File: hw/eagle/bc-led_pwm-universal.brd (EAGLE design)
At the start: 100 x 80 mm, 86 parts, among them T1 IRF7413, T10 IRF7413, T11 IRF7413, T12 IRF7413, T13 IRF7413, T14 IRF7413, T15 IRF7413, T16 IRF7413, T17 FDC6318P, T2 IRF7413, T3 IRF7413, T4 IRF7413, T5 IRF7413, T6 IRF7413, T7 IRF7413, T8 IRF7413, T9 IRF7413

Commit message: rotate core module to have convenient access to USB port, added pull-down resistors on output FETs, proper VDD_OFF handling and added power outage monitoring via P17
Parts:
- removed R2: 560R, resistor:R2012
- removed R3: 10k, resistor:R2012
- removed T17: FDC6318P, mixi:SSOT6
- added D2, D3, D4: B340A, diode:MELF-MLL41
- added R21, R22, R23, R24, R25, R26, R27, R28, R29, R30, R43, R44, R45, R46, R47, R48: 10k, resistor:R3216
- added R49: 560R, resistor:R3216
- R1: value 100k -> 560R; device resistor:R2012 -> resistor:R3216
- R4: device resistor:R2012 -> resistor:R3216
- moved R1 38.2 mm to (44.5, 54.6), turned to 90 degrees
- moved R4 32.0 mm to (88.9, 67.3)
- moved R8 26.2 mm to (43.2, 69.8), turned to 270 degrees
- moved R9 20.8 mm to (40.6, 69.8), turned to 270 degrees
- moved R19 14.2 mm to (34.3, 69.8), turned to 270 degrees
- moved R20 12.7 mm to (31.8, 69.8), turned to 270 degrees
- moved U$1 5.08 mm to (86.4, 53.3)
- moved D1 3.81 mm to (86.4, 38.1)
- moved L1 2.54 mm to (86.4, 34.3)
- moved CORE 0.27 mm to (27.6, 63.2), turned to 270 degrees
- moved R65 0.25 mm to (70.9, 21.6)
- moved R83 0.25 mm to (81.0, 21.6)
- moved R11 0.25 mm to (20.1, 21.6)
- moved R17 0.25 mm to (30.2, 21.6)
- moved R35 0.25 mm to (40.4, 21.6)
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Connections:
- removed net N$1: R1.2, T17.2, T17.5
- removed net N$3: R1.1, R2.2, R3.1, T17.1, T17.3
- new net N$14: D2.C, R4.2
- new net N$15: D3.C, R49.2
- net +3V3: now also D2.A, D3.A, D4.A, R1.2; no longer R4.2, T17.6
- net GND: now also R21.1, R22.1, R23.1, R24.1, R25.1, R26.1, R27.1, R28.1, R29.1, R30.1, R43.1, R44.1, R45.1, R46.1, R47.1, R48.1; no longer R3.2
- net N$10: now also R22.2
- net N$12: now also R24.2
- net N$2: now also R21.2
- net N$22: now also R25.2
- net N$24: now also R26.2
- net N$26: now also R27.2
- net N$28: now also R28.2
- net N$38: now also R29.2
- net N$40: now also R30.2
- net N$42: now also R43.2
- net N$44: now also R44.2
- net N$54: now also R45.2
- net N$56: now also R46.2
- net N$58: now also R47.2
- net N$60: now also R48.2
- net N$8: now also R23.2
- net P16: now also JP3.2
- net P17: now also R1.1; no longer JP3.2
- net VDD: now also D4.C; no longer T17.4
- net VDD_OFF_IN: now also R49.1; no longer R2.1
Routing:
- net BAT_OFF: track 63.1 -> 159.2 mm
- net N$15: track 0.00 -> 71.4 mm
- net P8: track 9.58 -> 74.6 mm
- net P14: track 86.3 -> 21.4 mm
- net P15: track 89.3 -> 24.7 mm
- net P7: track 5.77 -> 69.3 mm
- net P13: track 83.3 -> 21.4 mm
- net P6: track 5.77 -> 66.4 mm
- net P12: track 79.2 -> 21.4 mm
- net P5: track 15.8 -> 68.8 mm
- net P4: track 14.5 -> 66.8 mm
- net P3: track 5.46 -> 57.4 mm
- net P17: track 54.0 -> 2.83 mm
- net P9: track 8.84 -> 59.6 mm
- net P16: track 0.00 -> 50.6 mm, vias 0 -> 2
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
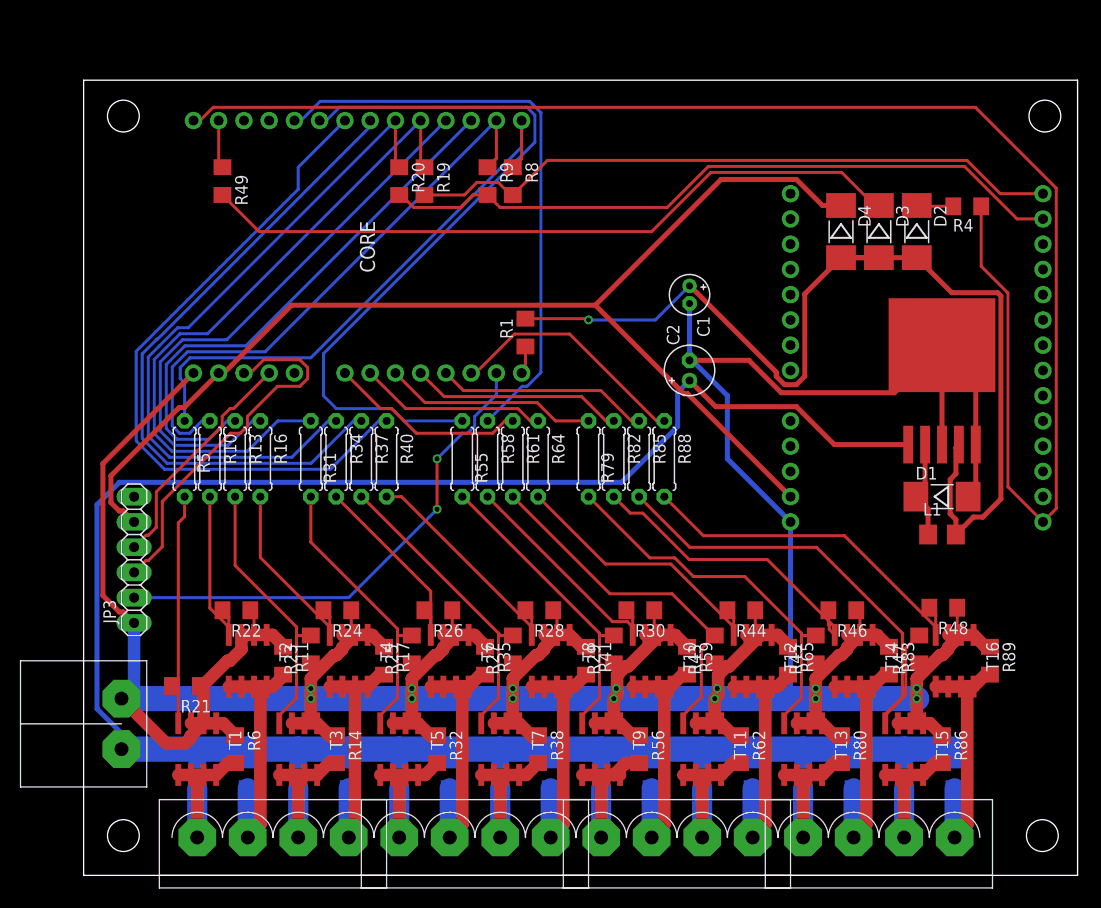
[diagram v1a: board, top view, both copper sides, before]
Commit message: added ground plane, reworked step-down
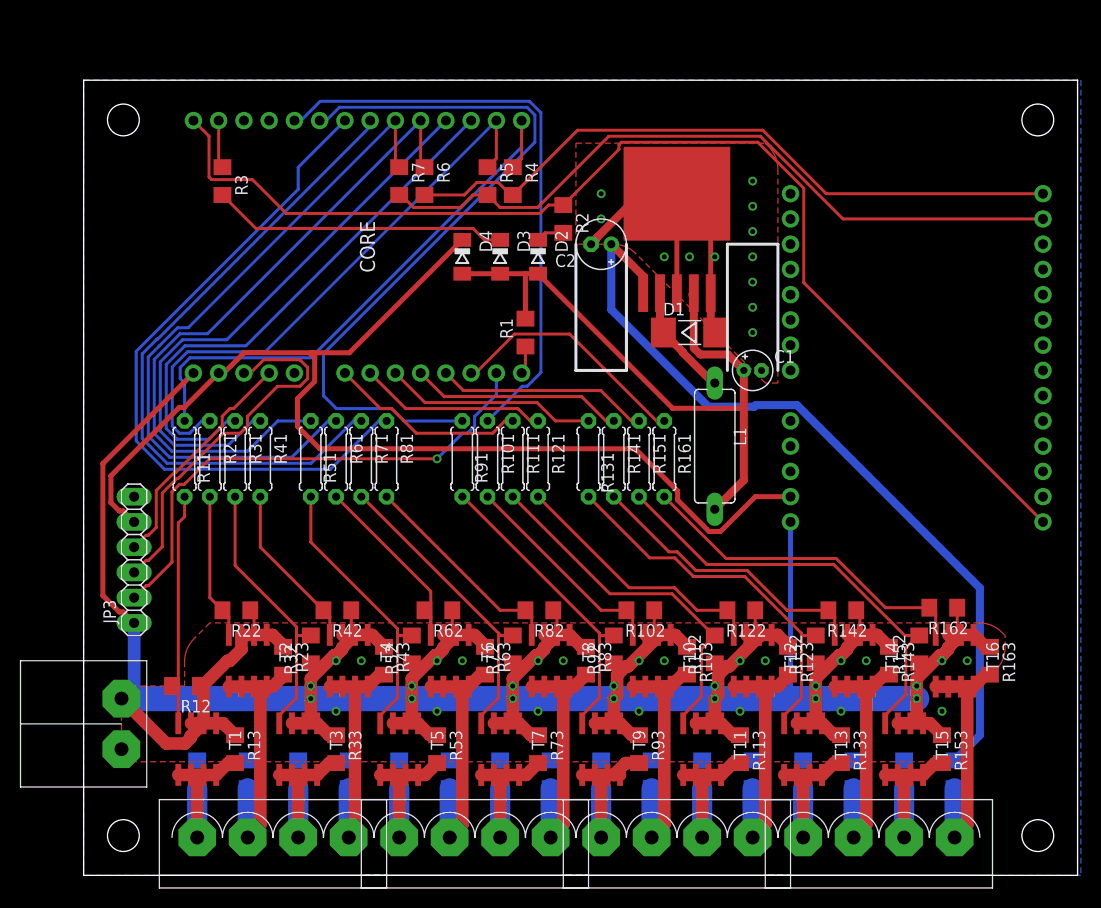
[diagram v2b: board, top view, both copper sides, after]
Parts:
- removed R10, R16, R40: 390R, resistor:0207/7
- removed R15, R17, R18, R19, R20, R35, R36, R8, R9: 0R, resistor:R3216
- removed R26, R28: 10k, resistor:R3216
- added R111, R121, R141, R51: 390R, resistor:0207/7
- added R112, R122: 10k, resistor:R3216
- added R113, R114, R134, R143, R144, R53, R54: 0R, resistor:R3216
- added R2: 560R, resistor:R3216
- D2, D3, D4: device diode:MELF-MLL41 -> diode:SOD80C
- L1: device eagle-ltspice:L3225P -> inductors:BC12
- R11, R41, R81: value 0R -> 390R; device resistor:R3216 -> resistor:0207/7
- R12, R32, R42, R62: value 0R -> 10k
- R13, R34, R5, R64: value 390R -> 0R; device resistor:0207/7 -> resistor:R3216
- R21: value 10k -> 390R; device resistor:R3216 -> resistor:0207/7
- R23, R24, R43, R44: value 10k -> 0R
- R4: value 560R -> 0R
- R82: value 390R -> 10k; device resistor:0207/7 -> resistor:R3216
- moved R7 63.1 mm to (31.8, 69.8), flipped to the top
- moved R6 60.2 mm to (34.3, 69.8)
- moved R81 52.6 mm to (30.5, 41.9), flipped to the top
- moved R4 45.8 mm to (43.2, 69.8), turned to 270 degrees
- moved R44 42.8 mm to (26.7, 10.2), flipped to the bottom, turned to 270 degrees
- moved R5 41.3 mm to (40.6, 69.8)
- moved R41 38.6 mm to (17.8, 41.9)
- moved D3 38.2 mm to (41.9, 62.2)
- moved D4 38.2 mm to (38.1, 62.2)
- moved D2 38.2 mm to (45.7, 62.2)
- moved R62 33.4 mm to (35.7, 26.7), turned to 180 degrees
- moved R43 33.3 mm to (30.2, 21.6), turned to 270 degrees
- moved R64 33.0 mm to (36.8, 10.2), flipped to the bottom
- moved R34 32.0 mm to (21.6, 10.2), flipped to the bottom
- moved U$1 30.7 mm to (59.7, 68.6)
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- renumbered R25 to R52, R27 to R72, R29 to R92, R30 to R102, R37 to R71, R38 to R73, R39 to R74, R45 to R132, R46 to R142, R47 to R152, R48 to R162, R49 to R3, R55 to R91, R56 to R93, R57 to R94, R58 to R101, R59 to R103, R60 to R104, R65 to R123, R66 to R124, R79 to R131, R80 to R133, R85 to R151, R86 to R153, R87 to R154, R88 to R161, R89 to R163, R90 to R164
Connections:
- net +12V: now also R114.1, R134.1, R14.1, R144.1, R24.1, R34.1, R44.1, R54.1, R64.1; no longer R12.1, R15.1, R18.1, R33.1, R36.1, R42.1, R63.1, R7.1, R81.1
- net BAT_OFF: now also R2.1; no longer R4.1
- net GND: now also R112.1, R113.1, R12.1, R122.1, R13.1, R143.1, R33.1, R42.1, R53.1, R63.1, R82.1; no longer R11.1, R14.1, R17.1, R21.1, R24.1, R26.1, R28.1, R35.1, R41.1, R44.1, R6.1
- net N$10: now also R21.2; no longer R10.2
- net N$11: now also R23.2, R24.2; no longer R11.2, R12.2
- net N$12: now also R41.2, R42.2; no longer R16.2, R24.2
- net N$13: now also R43.2, R44.2; no longer R17.2, R18.2
- net N$14: now also R2.2; no longer R4.2
- net N$2: now also R11.2, R12.2; no longer R21.2, R5.2
- net N$22: now also R51.2; no longer R31.2
- net N$23: now also R53.2, R54.2; no longer R32.2, R33.2
- net N$24: now also R61.2, R62.2; no longer R26.2, R34.2
- net N$25: now also R63.2, R64.2; no longer R35.2, R36.2
- net N$28: now also R81.2, R82.2; no longer R28.2, R40.2
- net N$29: now also R83.2, R84.2; no longer R41.2, R42.2
- net N$4: now also R13.2, R14.2; no longer R6.2, R7.2
- net N$42: now also R111.2, R112.2; no longer R43.2, R61.2
- net N$43: now also R113.2, R114.2; no longer R62.2, R63.2
- net N$44: now also R121.2, R122.2; no longer R44.2, R64.2
- net N$5: now also R5.2, R7.2; no longer R20.2, R9.2
- net N$55: now also R134.2; no longer R81.2
- net N$56: now also R141.2; no longer R82.2
- net N$57: now also R143.2, R144.2; no longer R83.2, R84.2
- net N$6: now also R4.2, R6.2; no longer R19.2, R8.2
- net N$8: now also R31.2, R32.2; no longer R13.2, R23.2
- net N$9: now also R33.2, R34.2; no longer R14.2, R15.2
- net P0: now also R11.1, R4.1; no longer R5.1, R8.1
- net P1: now also R21.1, R5.1; no longer R10.1, R9.1
- net P10: now also R111.1; no longer R61.1
- net P11: now also R121.1; no longer R64.1
- net P13: now also R141.1; no longer R82.1
- net P2: now also R31.1; no longer R13.1
- net P3: now also R41.1; no longer R16.1
- net P4: now also R51.1, R6.1; no longer R19.1, R31.1
- net P5: now also R61.1, R7.1; no longer R20.1, R34.1
- net P7: now also R81.1; no longer R40.1
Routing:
- net +12V: track 219.1 -> 80.1 mm
- net GND: track 434.7 -> 388.3 mm, vias 14 -> 47
- net BAT_OFF: track 159.2 -> 116.4 mm
- net N$15: track 71.4 -> 29.8 mm
- net +3V3: track 105.3 -> 65.3 mm, vias 1 -> 0
- net N$58: track 52.3 -> 44.3 mm
- net VDD: track 120.3 -> 115.8 mm
- net N$12: track 19.5 -> 16.8 mm
- net N$10: track 17.4 -> 14.7 mm
- net N$6: track 66.1 -> 68.6 mm
- net N$5: track 70.2 -> 72.7 mm
- net N$60: track 36.5 -> 34.3 mm
- net N$44: track 28.7 -> 26.5 mm
- net N$40: track 23.6 -> 21.4 mm
- net N$28: track 23.6 -> 21.4 mm
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- added copper zone on layer 1, net GND
- added copper zone on layer 16, net GND

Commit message: fixes from DRC
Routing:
- net +12V: track 80.1 -> 182.1 mm
- net GND: track 388.3 -> 383.7 mm
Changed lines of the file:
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@@
 <wire x1="62.860196875" y1="47.147190625" x2="53.086" y2="56.9213875" width="0.8128" layer="16"/>
 <wire x1="53.086" y1="56.9213875" x2="53.086" y2="63.5" width="0.8128" layer="16"/>
-<wire x1="82.55" y1="11.56" x2="87.63" y2="11.56" width="0" layer="19" extent="16-16"/>
-<wire x1="77.47" y1="11.56" x2="82.55" y2="11.56" width="0" layer="19" extent="16-16"/>
-<wire x1="72.39" y1="11.56" x2="77.47" y2="11.56" width="0" layer="19" extent="16-16"/>
-<wire x1="67.31" y1="11.56" x2="72.39" y2="11.56" width="0" layer="19" extent="16-16"/>
-<wire x1="62.23" y1="11.56" x2="67.31" y2="11.56" width="0" layer="19" extent="16-16"/>
-<wire x1="57.15" y1="11.56" x2="62.23" y2="11.56" width="0" layer="19" extent="16-16"/>
-<wire x1="52.07" y1="11.56" x2="57.15" y2="11.56" width="0" layer="19" extent="16-16"/>
-<wire x1="46.99" y1="11.56" x2="52.07" y2="11.56" width="0" layer="19" extent="16-16"/>
-<wire x1="41.91" y1="11.56" x2="46.99" y2="11.56" width="0" layer="19" extent="16-16"/>
-<wire x1="36.83" y1="11.56" x2="41.91" y2="11.56" width="0" layer="19" extent="16-16"/>
-<wire x1="31.75" y1="11.56" x2="36.83" y2="11.56" width="0" layer="19" extent="16-16"/>
-<wire x1="26.67" y1="11.56" x2="31.75" y2="11.56" width="0" layer="19" extent="16-16"/>
-<wire x1="21.59" y1="11.56" x2="26.67" y2="11.56" width="0" layer="19" extent="16-16"/>
-<wire x1="16.51" y1="11.56" x2="21.59" y2="11.56" width="0" layer="19" extent="16-16"/>
-<wire x1="11.43" y1="11.56" x2="16.51" y2="11.56" width="0" layer="19" extent="16-16"/>
-<wire x1="3.81" y1="12.7" x2="11.43" y2="11.56" width="0" layer="19" extent="16-16"/>
+<wire x1="3.81" y1="12.7" x2="11.43" y2="12.7" width="2.54" layer="16"/>
+<wire x1="11.43" y1="12.7" x2="16.51" y2="12.7" width="2.54" layer="16"/>
+<wire x1="16.51" y1="12.7" x2="21.59" y2="12.7" width="2.54" layer="16"/>
+<wire x1="21.59" y1="12.7" x2="26.67" y2="12.7" width="2.54" layer="16"/>
+<wire x1="26.67" y1="12.7" x2="31.75" y2="12.7" width="2.54" layer="16"/>
+<wire x1="31.75" y1="12.7" x2="36.83" y2="12.7" width="2.54" layer="16"/>
+<wire x1="36.83" y1="12.7" x2="41.91" y2="12.7" width="2.54" layer="16"/>
+<wire x1="41.91" y1="12.7" x2="46.99" y2="12.7" width="2.54" layer="16"/>
+<wire x1="46.99" y1="12.7" x2="52.07" y2="12.7" width="2.54" layer="16"/>
+<wire x1="52.07" y1="12.7" x2="57.15" y2="12.7" width="2.54" layer="16"/>
+<wire x1="57.15" y1="12.7" x2="62.23" y2="12.7" width="2.54" layer="16"/>
+<wire x1="62.23" y1="12.7" x2="67.31" y2="12.7" width="2.54" layer="16"/>
+<wire x1="67.31" y1="12.7" x2="72.39" y2="12.7" width="2.54" layer="16"/>
+<wire x1="72.39" y1="12.7" x2="77.47" y2="12.7" width="2.54" layer="16"/>
+<wire x1="77.47" y1="12.7" x2="82.55" y2="12.7" width="2.54" layer="16"/>
+<wire x1="87.63" y1="12.7" x2="82.55" y2="12.7" width="2.54" layer="16"/>
+<wire x1="11.43" y1="11.56" x2="11.43" y2="12.7" width="1.27" layer="16"/>
+<wire x1="16.51" y1="11.56" x2="16.51" y2="12.7" width="1.27" layer="16"/>
+<wire x1="21.59" y1="11.56" x2="21.59" y2="12.7" width="1.27" layer="16"/>
+<wire x1="26.67" y1="11.56" x2="26.67" y2="12.7" width="1.27" layer="16"/>
+<wire x1="31.75" y1="11.56" x2="31.75" y2="12.7" width="1.27" layer="16"/>
+<wire x1="36.83" y1="11.56" x2="36.83" y2="12.7" width="1.27" layer="16"/>
+<wire x1="41.91" y1="11.56" x2="41.91" y2="12.7" width="1.27" layer="16"/>
+<wire x1="46.99" y1="11.56" x2="46.99" y2="12.7" width="1.27" layer="16"/>
+<wire x1="52.07" y1="11.56" x2="52.07" y2="12.7" width="1.27" layer="16"/>
+<wire x1="57.15" y1="11.56" x2="57.15" y2="12.7" width="1.27" layer="16"/>
+<wire x1="62.23" y1="11.56" x2="62.23" y2="12.7" width="1.27" layer="16"/>
+<wire x1="67.31" y1="11.56" x2="67.31" y2="12.7" width="1.27" layer="16"/>
+<wire x1="72.39" y1="11.56" x2="72.39" y2="12.7" width="1.27" layer="16"/>
+<wire x1="77.47" y1="11.56" x2="77.47" y2="12.7" width="1.27" layer="16"/>
+<wire x1="82.55" y1="11.56" x2="82.55" y2="12.7" width="1.27" layer="16"/>
+<wire x1="87.63" y1="11.56" x2="87.63" y2="12.7" width="1.27" layer="16"/>
 </signal>
 <signal name="GND">
@@
 <wire x1="83.82" y1="15.935" x2="83.185" y2="15.3" width="1.27" layer="1"/>
 <wire x1="59.69" y1="58.58" x2="59.69" y2="68.58" width="0.508" layer="1"/>
-<wire x1="73.99" y1="18.72" x2="74.93" y2="17.78" width="0.508" layer="16"/>
 <wire x1="63.09" y1="58.58" x2="63.09" y2="65.18" width="0.508" layer="1"/>
 <wire x1="63.09" y1="65.18" x2="59.69" y2="68.58" width="0.508" layer="1"/>
@@
 <wire x1="10.2122875" y1="13.265" x2="8.325" y2="13.265" width="1.27" layer="1"/>
 <wire x1="8.325" y1="13.265" x2="3.81" y2="17.78" width="1.27" layer="1"/>
-<wire x1="63.754" y1="18.796" x2="63.754" y2="18.034" width="0.508" layer="1"/>
-<wire x1="63.754" y1="18.034" x2="63.5" y2="17.78" width="0.508" layer="1"/>
-<wire x1="53.594" y1="18.796" x2="53.594" y2="18.034" width="0.508" layer="1"/>
-<wire x1="53.594" y1="18.034" x2="53.34" y2="17.78" width="0.508" layer="1"/>
-<wire x1="83.82" y1="18.796" x2="83.82" y2="17.78" width="0.508" layer="1"/>
 <contactref element="R12" pad="1"/>
 <contactref element="R22" pad="1"/>
@@
 <wire x1="1.94" y1="28.1502875" x2="3.5932875" y2="26.497" width="0.508" layer="1"/>
 <wire x1="71.12" y1="35.56" x2="71.12" y2="17.78" width="0.508" layer="16"/>
-<polygon width="0.508" layer="16">
+<polygon width="0.508" layer="16" isolate="0.6096">
 <vertex x="0" y="80.01"/>
 <vertex x="100.33" y="80.01"/>
@@
 <wire x1="62.92333125" y1="34.5996" x2="59.7614" y2="37.76153125" width="0.508" layer="1"/>
 <wire x1="59.7614" y1="37.76153125" x2="59.7614" y2="38.65563125" width="0.508" layer="1"/>
-<wire x1="23.32291875" y1="52.5758" x2="22.86" y2="52.5758" width="0.508" layer="1"/>
 <wire x1="22.86" y1="52.5758" x2="16.1384" y2="52.5758" width="0.508" layer="1"/>
 <wire x1="21.5186" y1="45.16436875" x2="21.5186" y2="47.96188125" width="0.508" layer="1"/>
@@
 <contactref element="D4" pad="A"/>
 <contactref element="R1" pad="2"/>
-<wire x1="61.2346" y1="58.4246" x2="61.39" y2="58.58" width="0.8128" layer="1"/>
 <wire x1="66.421" y1="50.8" x2="64.8174" y2="52.4036" width="0.8128" layer="1"/>
 <wire x1="64.8174" y1="52.4036" x2="62.0424" y2="52.4036" width="0.8128" layer="1"/>

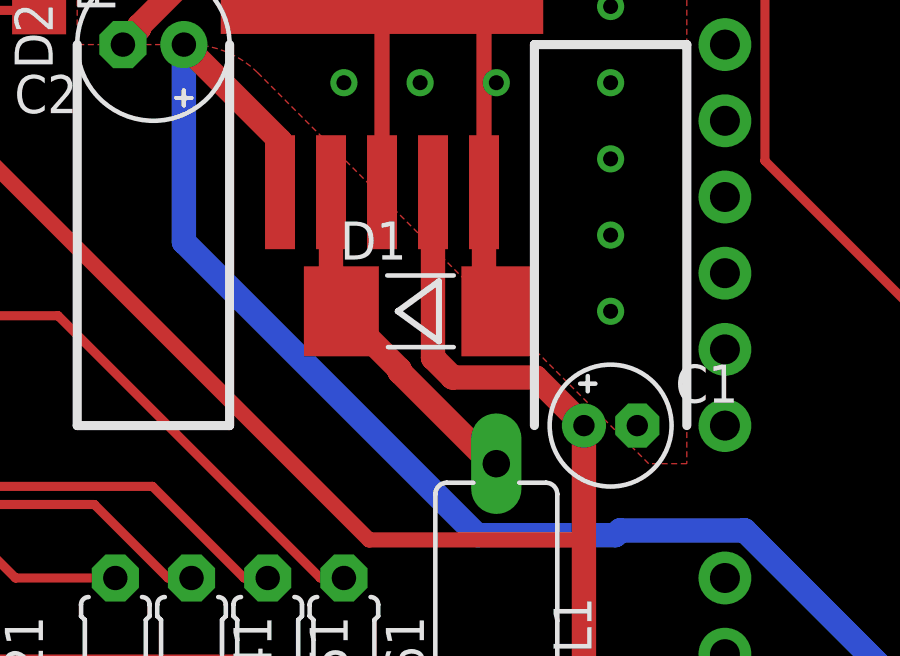
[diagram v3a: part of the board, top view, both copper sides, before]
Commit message: Changed 0R on FET gates, fixed symbols for schottky & inductor
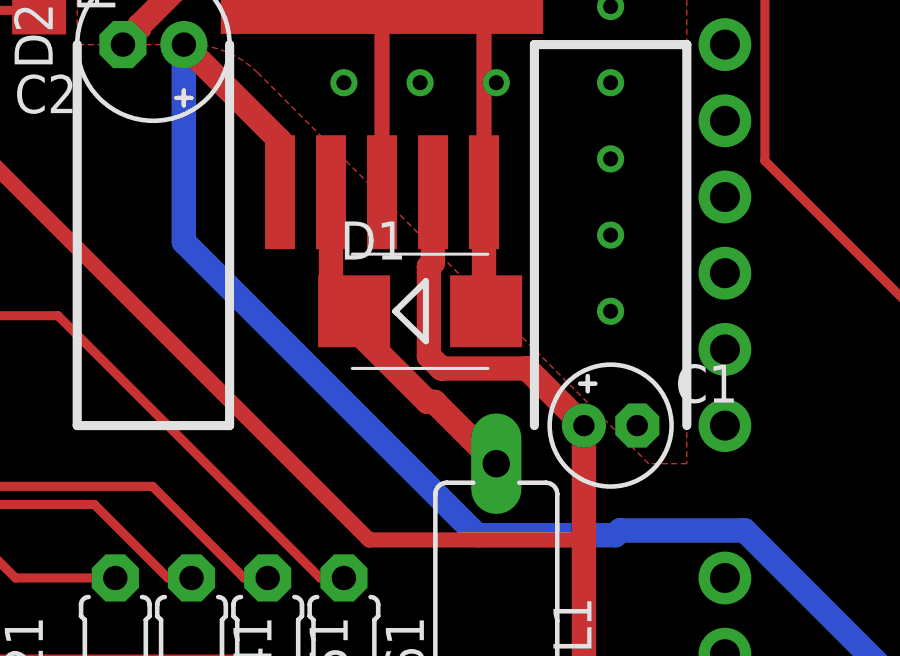
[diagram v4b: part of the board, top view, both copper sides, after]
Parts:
- D1: device diode:MELF-MLL41 -> diode:SMB
- D2, D3, D4: value B340A -> (none)
- L1: device inductors:BC12 -> mixi-inductors:BC12
- R101, R11, R111, R121, R131, R141, R151, R161, R21, R31, R41, R51, R61, R71, R81, R91: value 390R -> 0R

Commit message: onboard descriptions
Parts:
- moved R162 0.25 mm to (86.5, 26.7)
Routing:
- net GND: track 383.5 -> 383.3 mm, vias 47 -> 52
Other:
- board text added: "+5-24V"
- board text added: "0V"
- board text added: "Adafruit 16x 12-bit PWM - PCA9685 https://www.adafruit.com/product/815"
- board text added: "BATT"
- board text added: "uniPWM v1.0 for Hardwario TOWER https://github.com/mixicz/harwario-board-pwm"
